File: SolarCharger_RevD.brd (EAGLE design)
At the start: 85 x 78 mm, 132 parts, among them CON1 CON_4X200MIL, CON2 USB_BMULTICOMP, CON3 ICSP, CON4 CON_3X100MIL, CON5 CON_3X100MIL, CON6 CON_8X200MIL, CON7 CON_2X100MIL, IC1 MCP3428, IC10 AT45DB161E, IC11 TPS54428, IC12 MCP14A0153, IC13 MCP14A0153, IC2 INA213, IC3 MIC4605-1YM, IC4 INA213, IC5 PIC18F46J50, IC6 TS6001, IC7 LMT86, IC8 24AA16, IC9 TPS62120, Q1 NX3008NBKW, Q10 NTR4101PT1G, Q11 N-FET, Q12 N-FET, Q13 N-FET, Q14 N-FET, Q15 NX3008NBKW, Q2 PSMN6R0-30YL, Q3 NX3008NBKW, Q4 NTR4101PT1G, Q5 PSMN6R0-30YL, Q6 PSMN6R0-30YL, Q7 NX3008NBKW, Q8 NX3008NBKW, Q9 NX3008NBKW, X1 ABS07-120-32.768KHZ-T, X2 ABM3-8.000MHZ-D2Y-T, X3 USB_A, X4 USB_A

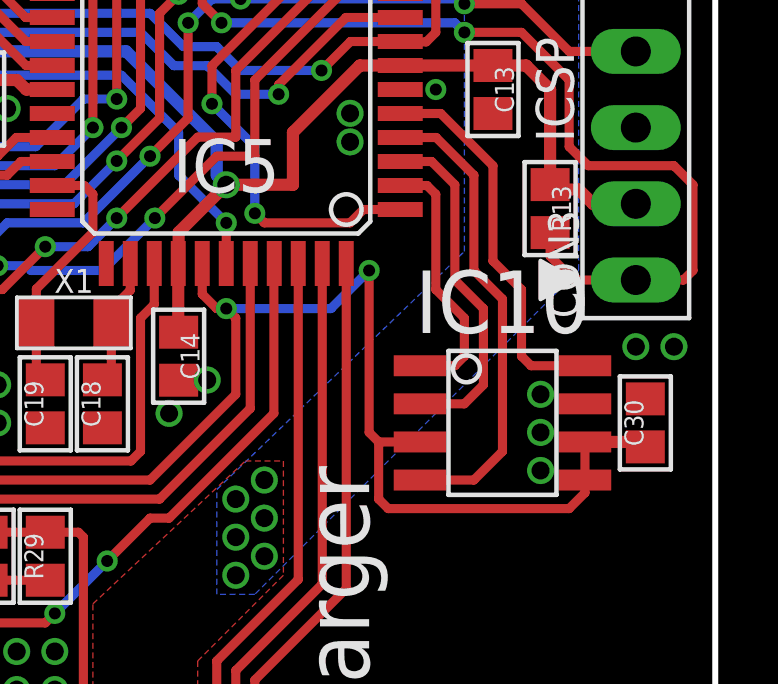
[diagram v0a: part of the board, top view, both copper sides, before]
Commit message: Flash now supplied directly from VCC
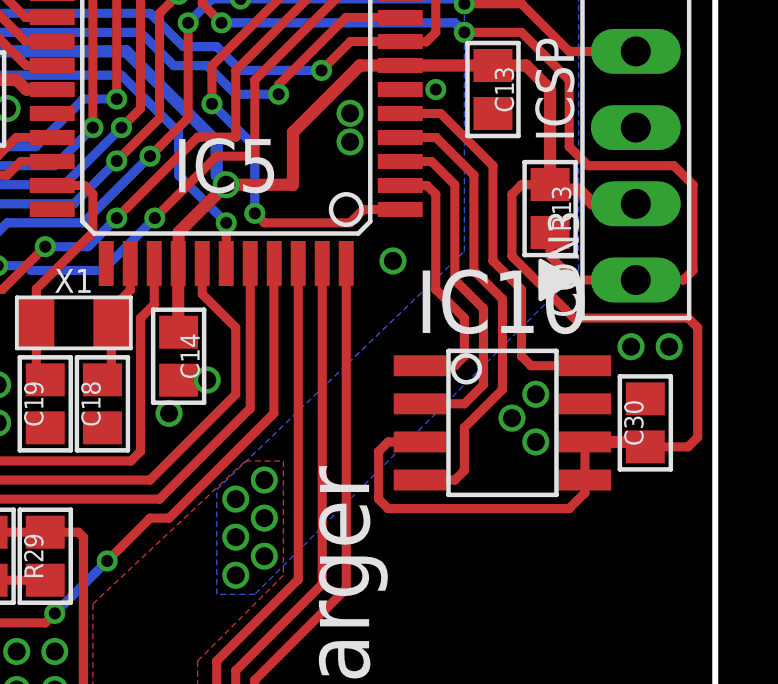
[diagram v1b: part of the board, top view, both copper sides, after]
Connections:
- net VCC: now also C30.1, IC10.3, IC10.5, IC10.6
- net VCC_HIGH: no longer C30.1, IC10.3, IC10.5, IC10.6
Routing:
- net VCC: track 134.5 -> 164.7 mm
- net VCC_HIGH: track 220.0 -> 194.4 mm, vias 12 -> 10
- net GND: vias 215 -> 216
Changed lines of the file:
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@@
 <via x="68.58" y="31.75" extent="1-16" drill="0.6"/>
 <via x="68.58" y="30.48" extent="1-16" drill="0.6"/>
-<via x="86.6775" y="28.8925" extent="1-16" drill="0.6"/>
-<via x="91.1225" y="33.02" extent="1-16" drill="0.6"/>
-<via x="89.8525" y="33.02" extent="1-16" drill="0.6"/>
-<via x="86.6775" y="31.4325" extent="1-16" drill="0.6"/>
-<via x="86.6775" y="30.1625" extent="1-16" drill="0.6"/>
+<via x="86.51875" y="29.845" extent="1-16" drill="0.6"/>
+<via x="90.96375" y="33.02" extent="1-16" drill="0.6"/>
+<via x="89.69375" y="33.02" extent="1-16" drill="0.6"/>
+<via x="86.51875" y="31.4325" extent="1-16" drill="0.6"/>
+<via x="85.725" y="30.63875" extent="1-16" drill="0.6"/>
 <via x="81.915" y="48.5775" extent="1-16" drill="0.6"/>
 <via x="83.185" y="48.5775" extent="1-16" drill="0.6"/>
@@
 <via x="48.26" y="45.72" extent="1-16" drill="0.6"/>
 <contactref element="IC10" pad="7"/>
+<via x="81.75625" y="35.8775" extent="1-16" drill="0.6"/>
 </signal>
 <signal name="VIN" class="1">
@@
 <wire x1="74.7975" y1="54.61" x2="74.8" y2="54.6075" width="0.4064" layer="1"/>
 <wire x1="61.9125" y1="48.26" x2="66.3575" y2="52.705" width="0.4064" layer="16"/>
+<contactref element="C30" pad="1"/>
+<contactref element="IC10" pad="6"/>
+<contactref element="IC10" pad="5"/>
+<wire x1="88.1575" y1="29.845" x2="88.1575" y2="28.575" width="0.3048" layer="1"/>
+<wire x1="88.1575" y1="29.845" x2="90.005" y2="29.845" width="0.4064" layer="1"/>
+<wire x1="90.005" y1="29.845" x2="90.17" y2="29.68" width="0.4064" layer="1"/>
+<contactref element="IC10" pad="3"/>
+<wire x1="81.28" y1="29.5275" x2="81.28" y2="27.94" width="0.3048" layer="1"/>
+<wire x1="81.28" y1="27.94" x2="81.5975" y2="27.6225" width="0.3048" layer="1"/>
+<wire x1="81.5975" y1="27.6225" x2="87.63" y2="27.6225" width="0.3048" layer="1"/>
+<wire x1="81.28" y1="29.5275" x2="81.5975" y2="29.845" width="0.3048" layer="1"/>
+<wire x1="81.5975" y1="29.845" x2="82.6575" y2="29.845" width="0.3048" layer="1"/>
+<wire x1="87.63" y1="27.6225" x2="88.1575" y2="28.15" width="0.3048" layer="1"/>
+<wire x1="88.1575" y1="28.15" x2="88.1575" y2="28.575" width="0.3048" layer="1"/>
+<wire x1="90.17" y1="29.68" x2="91.5925" y2="29.68" width="0.3048" layer="1"/>
+<wire x1="91.5925" y1="29.68" x2="91.91625" y2="30.00375" width="0.3048" layer="1"/>
+<wire x1="91.91625" y1="30.00375" x2="91.91625" y2="33.655" width="0.3048" layer="1"/>
+<wire x1="91.91625" y1="33.655" x2="91.59875" y2="33.9725" width="0.3048" layer="1"/>
+<wire x1="91.59875" y1="33.9725" x2="87.78875" y2="33.9725" width="0.3048" layer="1"/>
+<wire x1="87.78875" y1="33.9725" x2="85.725" y2="36.03625" width="0.3048" layer="1"/>
+<wire x1="85.725" y1="36.03625" x2="85.725" y2="38.1" width="0.3048" layer="1"/>
+<wire x1="85.725" y1="38.1" x2="86.0425" y2="38.4175" width="0.3048" layer="1"/>
+<wire x1="86.0425" y1="38.4175" x2="86.98875" y2="38.4175" width="0.3048" layer="1"/>
+<wire x1="86.98875" y1="38.4175" x2="86.995" y2="38.42375" width="0.3048" layer="1"/>
 <wire x1="47.3275" y1="39.37" x2="47.3275" y2="39.32" width="0" layer="19" extent="1-1"/>
 <wire x1="47.3775" y1="39.37" x2="47.3275" y2="39.37" width="0" layer="19" extent="1-1"/>
@@
 <contactref element="CON4" pad="1"/>
 <contactref element="IC6" pad="1"/>
-<contactref element="C30" pad="1"/>
 <contactref element="Q1" pad="1"/>
 <wire x1="19.3675" y1="52.86375" x2="19.3675" y2="43.815" width="0.3048" layer="1"/>
@@
 <wire x1="52.3875" y1="29.5275" x2="50.4825" y2="27.6225" width="0.3048" layer="1"/>
 <wire x1="50.4825" y1="27.6225" x2="50.4825" y2="22.5425" width="0.3048" layer="1"/>
-<via x="80.9625" y="35.56" extent="1-16" drill="0.4"/>
-<via x="76.2" y="34.29" extent="1-16" drill="0.4"/>
-<wire x1="76.2" y1="34.29" x2="79.6925" y2="34.29" width="0.3048" layer="16"/>
-<wire x1="79.6925" y1="34.29" x2="80.9625" y2="35.56" width="0.3048" layer="16"/>
-<wire x1="81.28" y1="29.845" x2="80.9625" y2="30.1625" width="0.3048" layer="1"/>
-<wire x1="80.9625" y1="30.1625" x2="80.9625" y2="35.56" width="0.3048" layer="1"/>
 <wire x1="76.5175" y1="31.4325" x2="73.66" y2="28.575" width="0.3048" layer="1"/>
 <wire x1="73.66" y1="28.575" x2="68.2625" y2="28.575" width="0.3048" layer="1"/>
@@
 <wire x1="35.08375" y1="21.11375" x2="32.7025" y2="18.7325" width="0.3048" layer="16"/>
 <wire x1="75.4" y1="35.7925" x2="75.4" y2="34.7725" width="0.3048" layer="1"/>
-<wire x1="75.4" y1="34.7725" x2="75.8825" y2="34.29" width="0.3048" layer="1"/>
-<wire x1="75.8825" y1="34.29" x2="76.2" y2="34.29" width="0.3048" layer="1"/>
-<wire x1="76.5175" y1="31.4325" x2="76.5175" y2="33.9725" width="0.3048" layer="1"/>
-<wire x1="76.5175" y1="33.9725" x2="76.2" y2="34.29" width="0.3048" layer="1"/>
+<wire x1="75.4" y1="34.7725" x2="76.5175" y2="33.655" width="0.3048" layer="1"/>
+<wire x1="76.5175" y1="31.4325" x2="76.5175" y2="33.655" width="0.3048" layer="1"/>
 <wire x1="16.145" y1="58.735" x2="15.2375" y2="58.735" width="0.3048" layer="1"/>
 <wire x1="15.2375" y1="58.735" x2="14.9225" y2="58.42" width="0.3048" layer="1"/>
@@
 <wire x1="46.355" y1="44.7675" x2="46.355" y2="45.0675" width="0.3048" layer="1"/>
 <wire x1="46.355" y1="45.0675" x2="46.42" y2="45.1325" width="0.3048" layer="1"/>
-<contactref element="IC10" pad="6"/>
-<contactref element="IC10" pad="5"/>
-<contactref element="IC10" pad="3"/>
-<wire x1="88.1575" y1="29.845" x2="88.1575" y2="28.575" width="0.3048" layer="1"/>
-<wire x1="81.28" y1="29.845" x2="81.28" y2="27.94" width="0.3048" layer="1"/>
-<wire x1="81.28" y1="27.94" x2="81.5975" y2="27.6225" width="0.3048" layer="1"/>
-<wire x1="81.5975" y1="27.6225" x2="87.63" y2="27.6225" width="0.3048" layer="1"/>
-<wire x1="81.28" y1="29.845" x2="82.6575" y2="29.845" width="0.3048" layer="1"/>
 <wire x1="56.99125" y1="43.33875" x2="57.15" y2="43.18" width="0.3048" layer="1"/>
-<wire x1="88.1575" y1="29.845" x2="90.005" y2="29.845" width="0.4064" layer="1"/>
-<wire x1="90.005" y1="29.845" x2="90.17" y2="29.68" width="0.4064" layer="1"/>
-<wire x1="87.63" y1="27.6225" x2="88.1575" y2="28.15" width="0.3048" layer="1"/>
-<wire x1="88.1575" y1="28.15" x2="88.1575" y2="28.575" width="0.3048" layer="1"/>
 </signal>
 <signal name="PGD/ENC_B">
@@
 <wire x1="85.4075" y1="34.6075" x2="84.455" y2="35.56" width="0.3048" layer="1"/>
 <wire x1="84.455" y1="35.56" x2="84.455" y2="38.735" width="0.3048" layer="1"/>
-<wire x1="85.4075" y1="34.6075" x2="85.4075" y2="29.5275" width="0.3048" layer="1"/>
-<wire x1="85.4075" y1="29.5275" x2="84.455" y2="28.575" width="0.3048" layer="1"/>
-<wire x1="84.455" y1="28.575" x2="82.6575" y2="28.575" width="0.3048" layer="1"/>
+<wire x1="85.4075" y1="34.6075" x2="85.4075" y2="31.59125" width="0.3048" layer="1"/>
+<wire x1="85.4075" y1="31.59125" x2="84.1375" y2="30.32125" width="0.3048" layer="1"/>
+<wire x1="84.1375" y1="30.32125" x2="84.1375" y2="28.8925" width="0.3048" layer="1"/>
+<wire x1="84.1375" y1="28.8925" x2="83.82" y2="28.575" width="0.3048" layer="1"/>
+<wire x1="83.82" y1="28.575" x2="82.6575" y2="28.575" width="0.3048" layer="1"/>
 </signal>
 <signal name="MISO">
